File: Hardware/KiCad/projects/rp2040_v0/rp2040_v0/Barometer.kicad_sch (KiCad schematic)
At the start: 10 parts, among them J14 Conn_02x06_Odd_Even, U6 BMP280

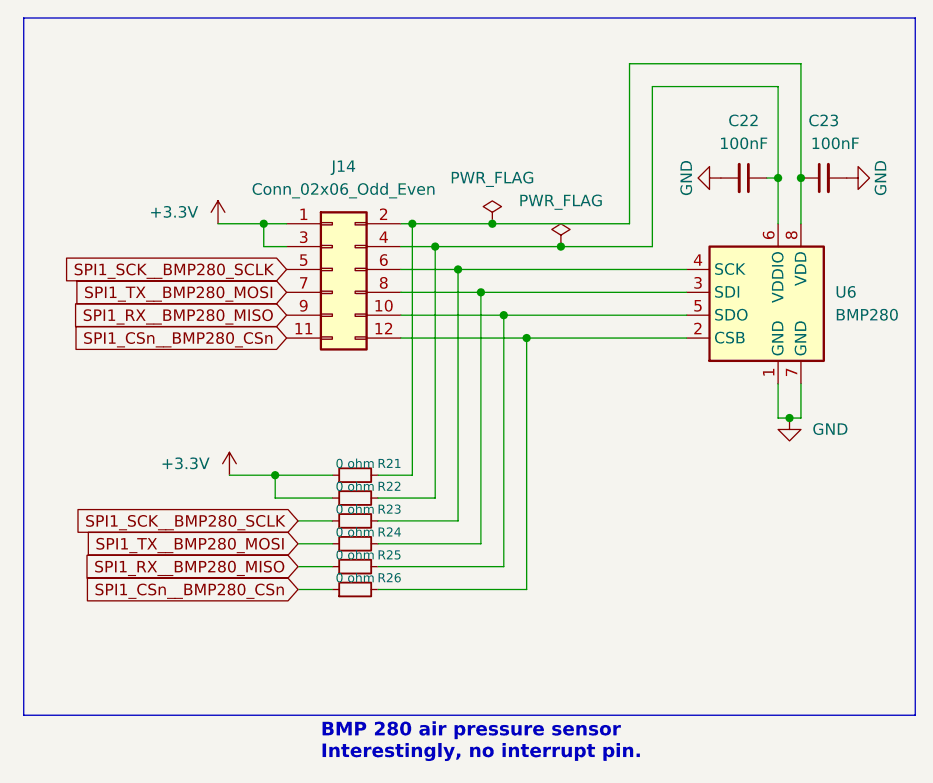
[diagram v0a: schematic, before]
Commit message: Change some header pin pinouts to make routing easier.
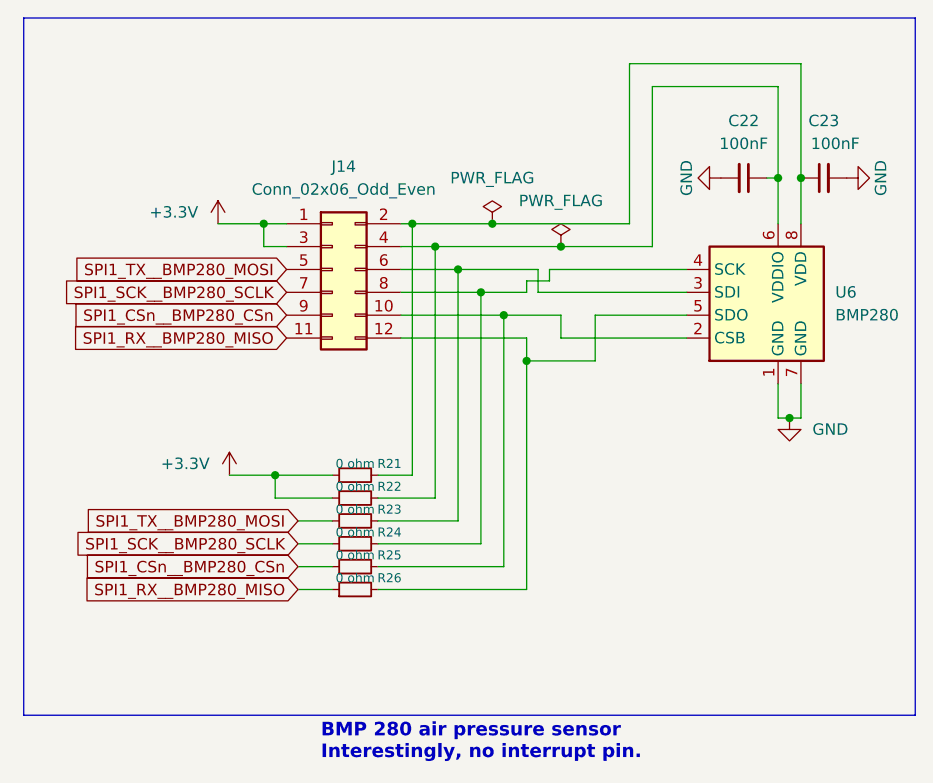
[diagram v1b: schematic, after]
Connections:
- net SPI1_CSn__BMP280_CSn: now also J14.9 (Pin_9), R25.1; no longer J14.11 (Pin_11), R26.1
- net SPI1_RX__BMP280_MISO: now also J14.11 (Pin_11), R26.1; no longer J14.9 (Pin_9), R25.1
- net SPI1_SCK__BMP280_SCLK: now also J14.7 (Pin_7), R24.1; no longer J14.5 (Pin_5), R23.1
- net SPI1_TX__BMP280_MOSI: now also J14.5 (Pin_5), R23.1; no longer J14.7 (Pin_7), R24.1
- net at J14.12 (Pin_12), R26.2: now also U6.5 (SDO); no longer U6.2 (CSB)
- net at J14.8 (Pin_8), R24.2: now also U6.4 (SCK); no longer U6.3 (SDI)
- net at J14.6 (Pin_6), R23.2: now also U6.3 (SDI); no longer U6.4 (SCK)
- net at J14.10 (Pin_10), R25.2: now also U6.2 (CSB); no longer U6.5 (SDO)
